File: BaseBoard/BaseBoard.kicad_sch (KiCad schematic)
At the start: 42 parts, among them CN1 PinStrip30, CN2 PinStrip30, CN3 PinStrip2x5, CN4 SDCardScocket, CN5 PowerJack, P1 USB_micro_B_female, U1 AP2112_R5A_SOT_89-5, U2 ATSAMD51J19, U3 FT232RL, Y1 32K768Hz

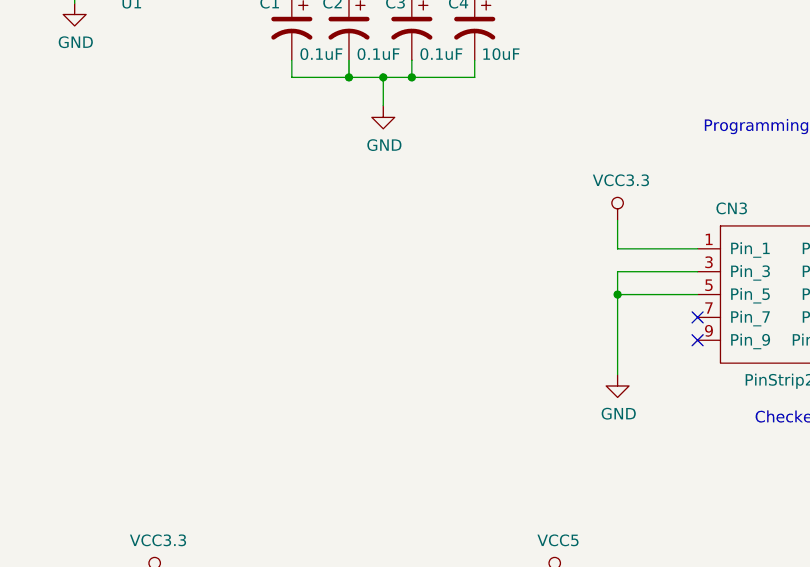
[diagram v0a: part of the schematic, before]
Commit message: Added JTAG to SWD equivalence in BaseBoard schematics
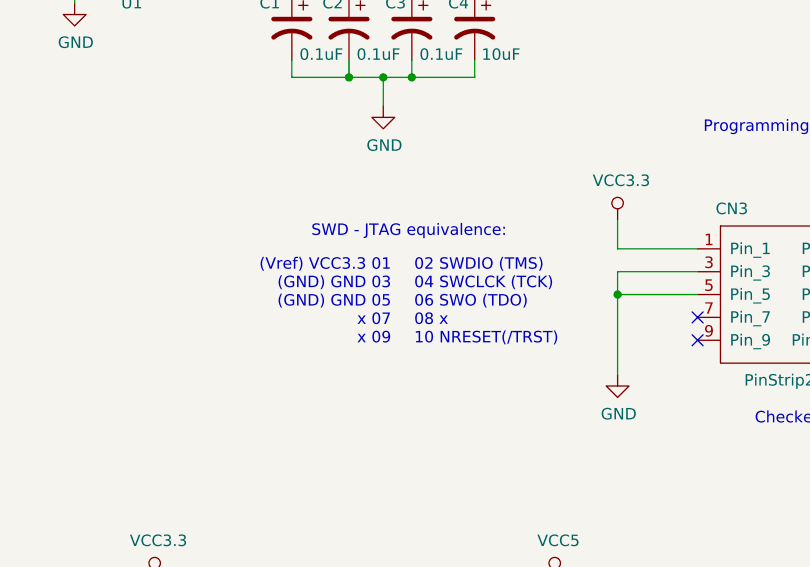
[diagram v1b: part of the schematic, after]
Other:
- note added: "(Vref) VCC3.3 01 (GND) GND 03 (GND) GND 05 x 07 x 09"
- note added: "02 SWDIO (TMS) 04 SWCLCK (TCK) 06 SWO (TDO) 08 x 10 NRESET(/TRST)"
- note added: "SWD - JTAG equivalence:"
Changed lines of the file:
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@@
     (effects (font (size 1.27 1.27)) (justify left bottom))
+  )
+  (text "\n(Vref) VCC3.3 01\n(GND) GND 03\n(GND) GND 05\nx 07\nx 09"
+    (at 65.024 95.25 180)
+    (effects (font (size 1.27 1.27)) (justify right bottom))
   )
   (text "Checked!\n" (at 44.45 35.56 0)
@@
   )
   (text "Checked!\n" (at 321.31 186.055 0)
+    (effects (font (size 1.27 1.27)) (justify left bottom))
+  )
+  (text "\n02 SWDIO (TMS)\n04 SWCLCK (TCK)\n06 SWO (TDO)\n08 x\n10 NRESET(/TRST)"
+    (at 67.564 95.25 0)
     (effects (font (size 1.27 1.27)) (justify left bottom))
   )
@@
     (effects (font (size 1.27 1.27)) (justify left bottom))
   )
+  (text "SWD - JTAG equivalence:" (at 56.134 83.312 0)
+    (effects (font (size 1.27 1.27)) (justify left bottom))
+  )
